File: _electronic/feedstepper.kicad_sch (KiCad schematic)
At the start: 11 parts

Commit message: BETA first upload
nothing major done here:
* updated KiCAD files to v9
* removed alternative 6v feed-in. The proposed buck converter is fine.
* added to all components LCSC component IDs. With this, exporting the project as gerber files also automatically creates correct BOM for JLCPCB manufacturing
*
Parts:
- C_STP1: LCSC (none) -> C96446
- D_STP1, D_STP2, D_STP3: LCSC (none) -> C2290
- J_28byj-48-12v_1: LCSC (none) -> C492404
- R_STP1, R_STP2, R_STP3, R_STP4: LCSC (none) -> C23186
- U_STP1: LCSC (none) -> C7512
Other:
- title: E-TKT v1.0 -> E-TKT v2.0 BETA

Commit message: JLC export added, LCSC numbers updated
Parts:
- D_STP4: LCSC (none) -> C2290
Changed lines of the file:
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@@
 			)
 		)
-		(property "LCSC" ""
+		(property "LCSC" "C2290"
 			(at 162.56 104.14 90)
 			(effects

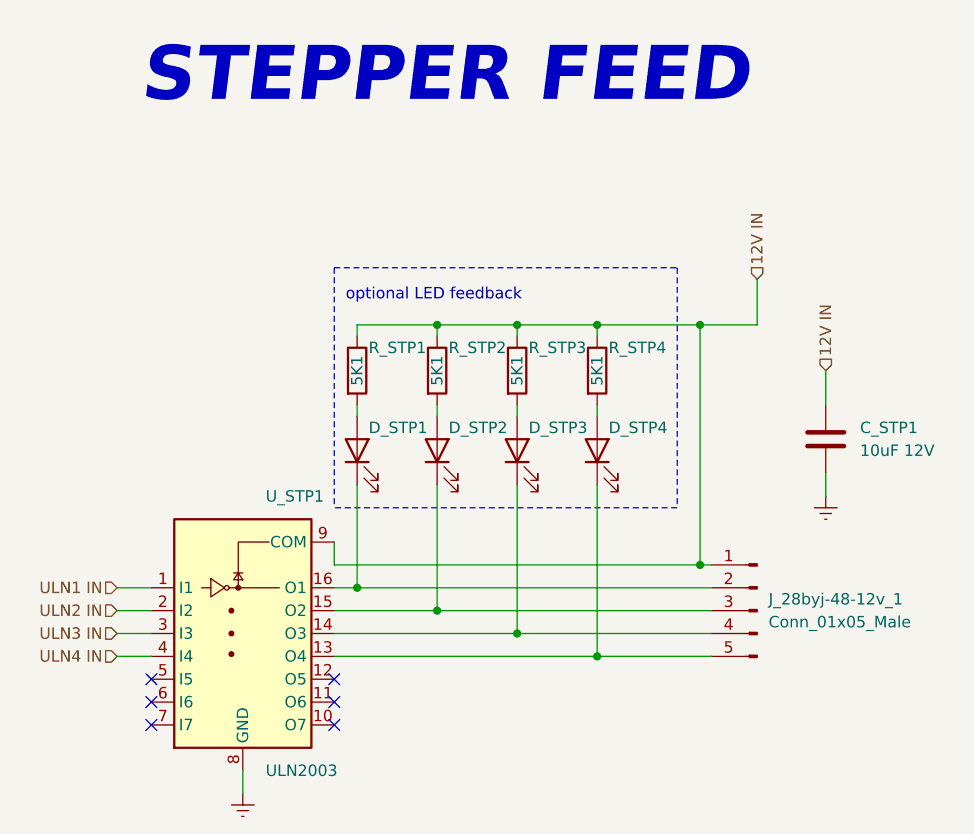
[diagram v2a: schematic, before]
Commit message: Updated layout of schematic symbol's text
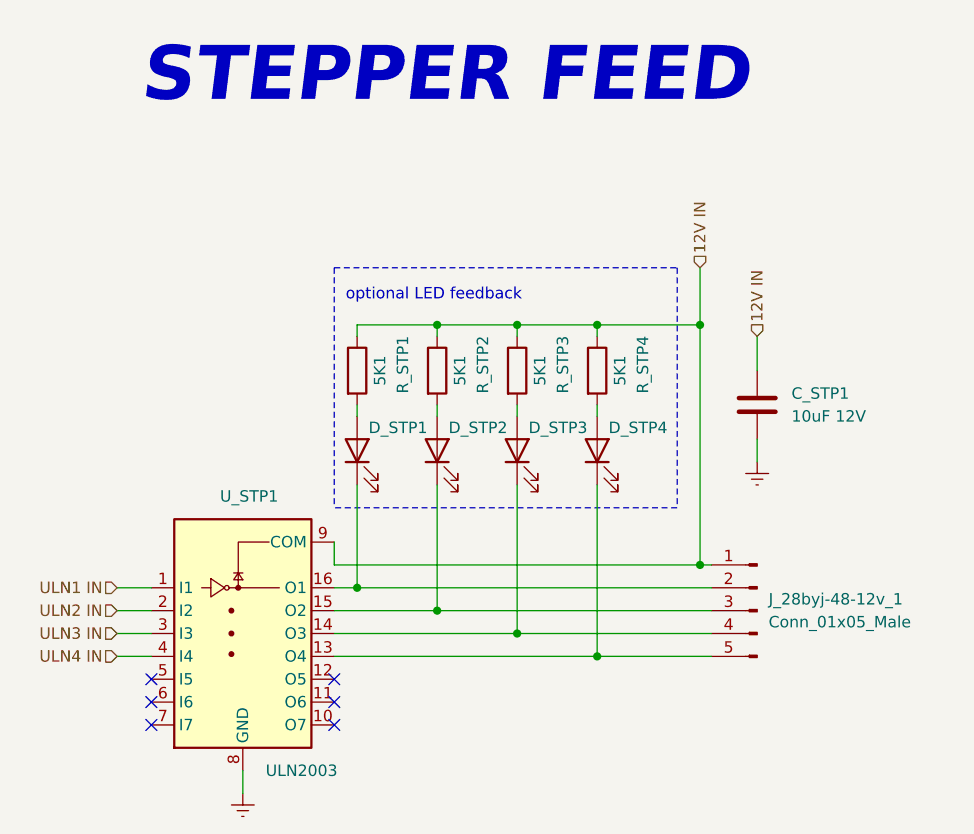
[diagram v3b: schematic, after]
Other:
- moved on the sheet: C_STP1
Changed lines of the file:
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@@
 	(wire
 		(pts
-			(xy 187.96 109.22) (xy 187.96 106.68)
+			(xy 180.34 105.41) (xy 180.34 102.87)
 		)
 		(stroke
@@
 	(wire
 		(pts
-			(xy 180.34 90.17) (xy 173.99 90.17)
-		)
-		(stroke
-			(width 0)
-			(type default)
-		)
-	)
-	(wire
-		(pts
 			(xy 162.56 127) (xy 175.26 127)
 		)
@@
 	(wire
 		(pts
-			(xy 187.96 95.25) (xy 187.96 99.06)
+			(xy 180.34 91.44) (xy 180.34 95.25)
 		)
 		(stroke
@@
 	(wire
 		(pts
-			(xy 180.34 85.09) (xy 180.34 90.17)
+			(xy 173.99 83.82) (xy 173.99 90.17)
 		)
 		(stroke
@@
 	(hierarchical_label "12V IN"
 		(shape input)
-		(at 180.34 85.09 90)
+		(at 173.99 83.82 90)
 		(effects
 			(font
@@
 	(hierarchical_label "12V IN"
 		(shape input)
-		(at 187.96 95.25 90)
+		(at 180.34 91.44 90)
 		(effects
 			(font
@@
 	(symbol
 		(lib_id "power:GNDREF")
-		(at 187.96 109.22 0)
+		(at 180.34 105.41 0)
 		(unit 1)
 		(exclude_from_sim no)
@@
 		(dnp no)
 		(property "Reference" "#PWR0169"
-			(at 187.96 115.57 0)
+			(at 180.34 111.76 0)
 			(effects
 				(font
@@
 		)
 		(property "Value" "GNDREF"
-			(at 187.96 114.3 0)
+			(at 180.34 110.49 0)
 			(effects
 				(font
@@
 		)
 		(property "Footprint" ""
-			(at 187.96 109.22 0)
+			(at 180.34 105.41 0)
 			(effects
 				(font
@@
 		)
 		(property "Datasheet" ""
-			(at 187.96 109.22 0)
+			(at 180.34 105.41 0)
 			(effects
 				(font
@@
 		)
 		(property "Description" ""
-			(at 187.96 109.22 0)
+			(at 180.34 105.41 0)
 			(effects
 				(font
@@
 		(dnp no)
 		(property "Reference" "R_STP3"
-			(at 154.94 92.7099 0)
+			(at 158.75 97.79 90)
 			(effects
 				(font
@@
 		)
 		(property "Value" "5K1"
-			(at 153.67 95.25 90)
+			(at 156.21 95.25 90)
 			(effects
 				(font
@@
 		(dnp no)
 		(property "Reference" "R_STP4"
-			(at 163.83 92.7099 0)
+			(at 167.64 97.79 90)
 			(effects
 				(font
@@
 		)
 		(property "Value" "5K1"
-			(at 162.56 95.25 90)
+			(at 165.1 95.25 90)
 			(effects
 				(font
@@
 		(dnp no)
 		(property "Reference" "R_STP1"
-			(at 137.16 92.71 0)
+			(at 140.97 97.79 90)
 			(effects
 				(font
@@
 		)
 		(property "Value" "5K1"
-			(at 135.89 95.25 90)
+			(at 138.43 95.25 90)
 			(effects
 				(font
@@
 		(dnp no)
 		(property "Reference" "R_STP2"
-			(at 146.05 92.71 0)
+			(at 149.86 97.79 90)
 			(effects
 				(font
@@
 		)
 		(property "Value" "5K1"
-			(at 144.78 95.25 90)
+			(at 147.32 95.25 90)
 			(effects
 				(font
@@
 		(dnp no)
 		(property "Reference" "U_STP1"
-			(at 125.73 109.22 0)
+			(at 120.65 109.22 0)
 			(effects
 				(font
@@
 	(symbol
 		(lib_id "Device:C")
-		(at 187.96 102.87 180)
+		(at 180.34 99.06 180)
 		(unit 1)
 		(exclude_from_sim no)
@@
 		(dnp no)
 		(property "Reference" "C_STP1"
-			(at 191.77 101.6 0)
+			(at 184.15 97.79 0)
 			(effects
 				(font
@@
 		)
 		(property "Value" "10uF 12V"
-			(at 191.77 104.14 0)
+			(at 184.15 100.33 0)
 			(effects
 				(font
@@
 		)
 		(property "Footprint" "Capacitor_SMD:C_0603_1608Metric_Pad1.08x0.95mm_HandSolder"
-			(at 186.9948 99.06 0)
+			(at 179.3748 95.25 0)
 			(effects
 				(font
@@
 		)
 		(property "Datasheet" "https://product.tdk.com/system/files/dam/doc/product/capacitor/ceramic/mlcc/catalog/mlcc_commercial_general_en.pdf?ref_disty=mouser"
-			(at 187.96 102.87 0)
+			(at 180.34 99.06 0)
 			(effects
 				(font
@@
 		)
 		(property "Description" "Decouple"
-			(at 187.96 102.87 0)
+			(at 180.34 99.06 0)
 			(effects
 				(font
@@
 		)
 		(property "#" "GRM188Z71A106KA73D"
-			(at 193.04 102.87 0)
+			(at 185.42 99.06 0)
 			(effects
 				(font
@@
 		)
 		(property "Group" "28BYJ-48 12V"
-			(at 187.96 102.87 0)
+			(at 180.34 99.06 0)
 			(effects
 				(font
@@
 		)
 		(property "Obs" "wes"
-			(at 187.96 102.87 0)
+			(at 180.34 99.06 0)
 			(effects
 				(font
@@
 		)
 		(property "Mouser" "OK"
-			(at 187.96 102.87 0)
+			(at 180.34 99.06 0)
 			(effects
 				(font
@@
 		)
 		(property "LCSC" "C96446"
-			(at 187.96 102.87 0)
-			(effects
-				(font
+			(at 180.34 99.06 0)
+			(effects
+				(font
